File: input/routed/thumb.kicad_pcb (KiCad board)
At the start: 2 copper layers, 36 x 51 mm, 19 parts, among them T1 Flactyl 4.0 (thumb), T2 x, T3 y

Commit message: 4.1
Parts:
- removed H3: , MountingHole_1mm_M2
- T1: value Flactyl 4.0 (thumb) -> Flactyl 4.1 (thumb)
- moved H2 25.6 mm to (9.00, 0.00)
- moved H1 25.5 mm to (9.00, -34.0)
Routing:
- net C6: track 57.9 -> 54.8 mm

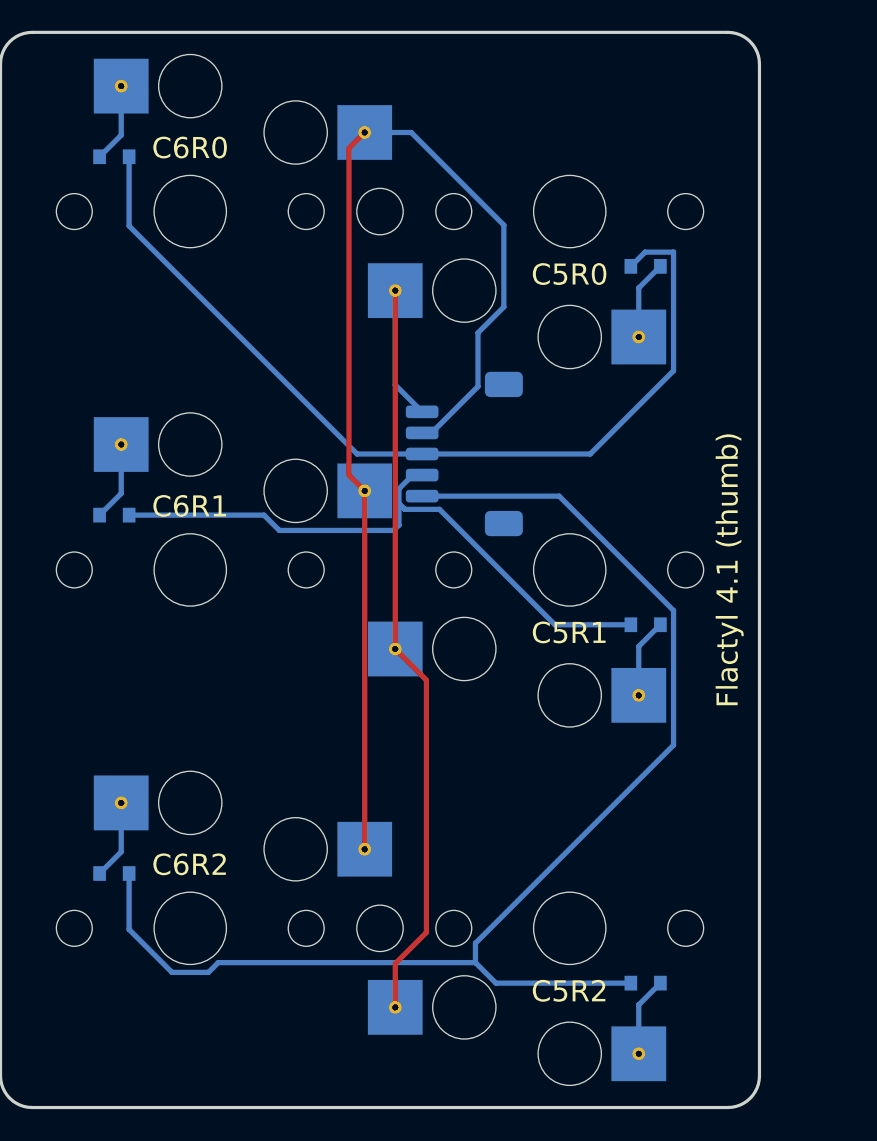
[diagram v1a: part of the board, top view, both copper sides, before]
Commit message: Thumb connector move
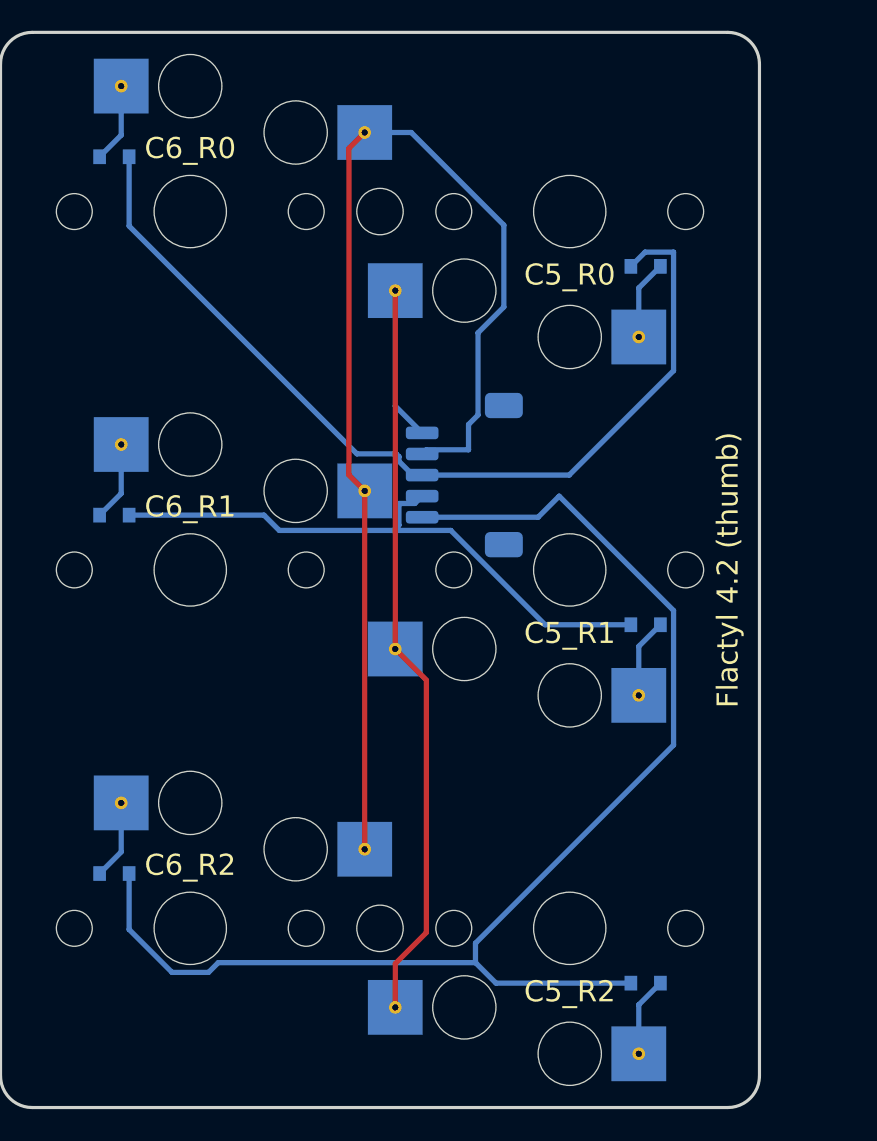
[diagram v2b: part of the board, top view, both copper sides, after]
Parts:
- T1: value Flactyl 4.1 (thumb) -> Flactyl 4.2 (thumb)
- moved JC1 1.00 mm to (13.0, -21.5)
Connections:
- net C5R0D renamed C5_R0D
- net C5R1D renamed C5_R1D
- net C5R2D renamed C5_R2D
- net C6R0D renamed C6_R0D
- net C6R1D renamed C6_R1D
- net C6R2D renamed C6_R2D
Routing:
- net C6: track 54.8 -> 56.7 mm
- net R1: track 29.7 -> 28.6 mm
- net C5: track 41.5 -> 42.5 mm
- net R0: track 43.2 -> 44.1 mm
